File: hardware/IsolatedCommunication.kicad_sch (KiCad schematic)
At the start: 4 parts, among them U13 LTC6820IMS

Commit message: added additional USB port and overall board update
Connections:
- net MSIO renamed MISO
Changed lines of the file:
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@@
     (effects (font (size 1.27 1.27)) (justify right))
   )
-  (hierarchical_label "MSIO" (shape output) (at 118.745 85.725 180)
+  (hierarchical_label "MISO" (shape output) (at 118.745 85.725 180)
     (effects (font (size 1.27 1.27)) (justify right))
   )
@@
   (symbol (lib_id "power:+3.3V") (at 120.015 78.105 0)
     (in_bom yes) (on_board yes)
-    (property "Reference" "#PWR?" (id 0) (at 120.015 81.915 0)
+    (property "Reference" "#PWR0144" (id 0) (at 120.015 81.915 0)
       (effects (font (size 1.27 1.27)) hide)
     )
@@
   (symbol (lib_id "power:GND") (at 145.415 107.95 0)
     (in_bom yes) (on_board yes)
-    (property "Reference" "#PWR?" (id 0) (at 145.415 114.3 0)
+    (property "Reference" "#PWR0143" (id 0) (at 145.415 114.3 0)
       (effects (font (size 1.27 1.27)) hide)
     )
@@
   (symbol (lib_id "power:+3.3V") (at 142.875 78.105 0)
     (in_bom yes) (on_board yes)
-    (property "Reference" "#PWR?" (id 0) (at 142.875 81.915 0)
+    (property "Reference" "#PWR0145" (id 0) (at 142.875 81.915 0)
       (effects (font (size 1.27 1.27)) hide)
     )

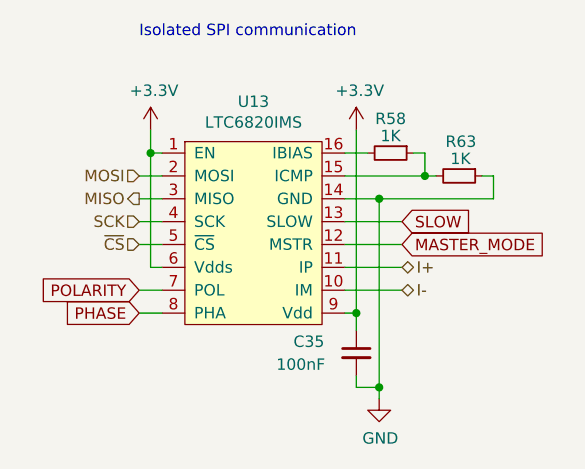
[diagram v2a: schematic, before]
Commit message: Schematic readability update
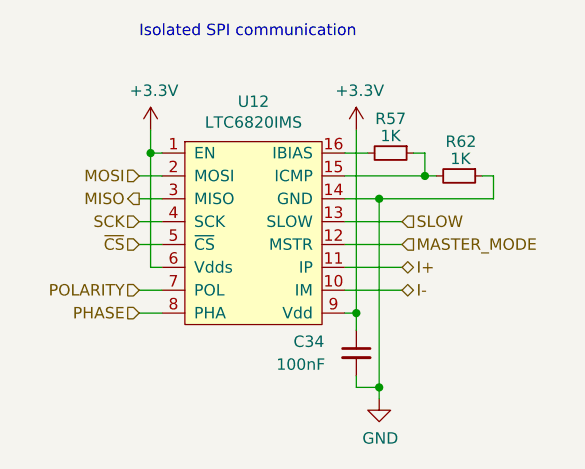
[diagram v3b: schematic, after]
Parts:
- renumbered C35 to C34, R58 to R57, R63 to R62, U13 to U12
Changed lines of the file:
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@@
     (effects (font (size 1.27 1.27)) (justify left bottom))
   )
-  (global_label "SLOW" (shape input) (at 147.955 88.265 0) (fields_autoplaced)
+  (hierarchical_label "SLOW" (shape input) (at 147.955 88.265 0)
     (effects (font (size 1.27 1.27)) (justify left))
-    (property "Intersheet References" "${INTERSHEET_REFS}" (id 0) (at 155.2987 88.1856 0)
-      (effects (font (size 1.27 1.27)) (justify left) hide)
-    )
-  )
-  (global_label "PHASE" (shape input) (at 118.745 98.425 180) (fields_autoplaced)
-    (effects (font (size 1.27 1.27)) (justify right))
-    (property "Intersheet References" "${INTERSHEET_REFS}" (id 0) (at 110.3732 98.3456 0)
-      (effects (font (size 1.27 1.27)) (justify right) hide)
-    )
-  )
-  (global_label "MASTER_MODE" (shape input) (at 147.955 90.805 0) (fields_autoplaced)
-    (effects (font (size 1.27 1.27)) (justify left))
-    (property "Intersheet References" "${INTERSHEET_REFS}" (id 0) (at 163.584 90.7256 0)
-      (effects (font (size 1.27 1.27)) (justify left) hide)
-    )
-  )
-  (global_label "POLARITY" (shape input) (at 118.745 95.885 180) (fields_autoplaced)
-    (effects (font (size 1.27 1.27)) (justify right))
-    (property "Intersheet References" "${INTERSHEET_REFS}" (id 0) (at 107.7727 95.8056 0)
-      (effects (font (size 1.27 1.27)) (justify right) hide)
-    )
   )
   (hierarchical_label "SCK" (shape input) (at 118.745 88.265 180)
@@
     (effects (font (size 1.27 1.27)) (justify right))
   )
+  (hierarchical_label "MASTER_MODE" (shape input) (at 147.955 90.805 0)
+    (effects (font (size 1.27 1.27)) (justify left))
+  )
   (hierarchical_label "MOSI" (shape input) (at 118.745 83.185 180)
     (effects (font (size 1.27 1.27)) (justify right))
   )
+  (hierarchical_label "POLARITY" (shape input) (at 118.745 95.885 180)
+    (effects (font (size 1.27 1.27)) (justify right))
+  )
   (hierarchical_label "MISO" (shape output) (at 118.745 85.725 180)
+    (effects (font (size 1.27 1.27)) (justify right))
+  )
+  (hierarchical_label "PHASE" (shape input) (at 118.745 98.425 180)
     (effects (font (size 1.27 1.27)) (justify right))
   )
@@
   (symbol (lib_id "power:+3.3V") (at 120.015 78.105 0)
     (in_bom yes) (on_board yes)
-    (property "Reference" "#PWR0144" (id 0) (at 120.015 81.915 0)
+    (property "Reference" "#PWR0141" (id 0) (at 120.015 81.915 0)
       (effects (font (size 1.27 1.27)) hide)
     )
@@
   (symbol (lib_id "power:GND") (at 145.415 107.95 0)
     (in_bom yes) (on_board yes)
-    (property "Reference" "#PWR0143" (id 0) (at 145.415 114.3 0)
+    (property "Reference" "#PWR0140" (id 0) (at 145.415 114.3 0)
       (effects (font (size 1.27 1.27)) hide)
     )
@@
   (symbol (lib_id "PUTM_EV_BMS_library:LTC6820IMS") (at 131.445 89.535 0)
     (in_bom yes) (on_board yes)
-    (property "Reference" "U13" (id 0) (at 131.445 74.93 0))
+    (property "Reference" "U12" (id 0) (at 131.445 74.93 0))
     (property "Value" "LTC6820IMS" (id 1) (at 131.445 77.2414 0))
     (property "Footprint" "Package_SO:MSOP-16_3x4.039mm_P0.5mm" (id 2) (at 131.445 103.505 0)
@@
   (symbol (lib_id "power:+3.3V") (at 142.875 78.105 0)
     (in_bom yes) (on_board yes)
-    (property "Reference" "#PWR0145" (id 0) (at 142.875 81.915 0)
+    (property "Reference" "#PWR0142" (id 0) (at 142.875 81.915 0)
       (effects (font (size 1.27 1.27)) hide)
     )
@@
   (symbol (lib_id "Device:R_Small") (at 154.305 83.185 270)
     (in_bom yes) (on_board yes)
-    (property "Reference" "R63" (id 0) (at 156.21 79.375 90)
+    (property "Reference" "R62" (id 0) (at 156.21 79.375 90)
       (effects (font (size 1.27 1.27)) (justify right))
     )
@@
   (symbol (lib_id "Device:R_Small") (at 146.685 80.645 270)
     (in_bom yes) (on_board yes)
-    (property "Reference" "R58" (id 0) (at 146.685 76.835 90))
+    (property "Reference" "R57" (id 0) (at 146.685 76.835 90))
     (property "Value" "1K" (id 1) (at 146.685 78.74 90))
     (property "Footprint" "Resistor_SMD:R_0603_1608Metric" (id 2) (at 146.685 80.645 0)
@@
   (symbol (lib_id "Device:C_Small") (at 142.875 102.87 0)
     (in_bom yes) (on_board yes)
-    (property "Reference" "C35" (id 0) (at 135.89 101.6 0)
+    (property "Reference" "C34" (id 0) (at 135.89 101.6 0)
       (effects (font (size 1.27 1.27)) (justify left))
     )

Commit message: finished pcb layout, started routing, changed 2 layered board to 4 layered'
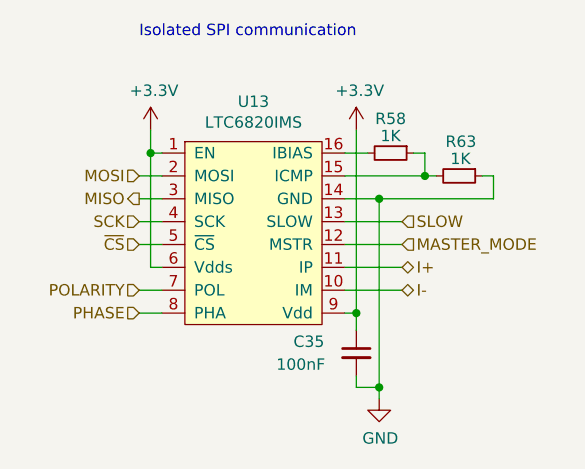
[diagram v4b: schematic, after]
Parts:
- renumbered C34 to C35, R57 to R58, R62 to R63, U12 to U13
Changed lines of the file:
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@@
   (symbol (lib_id "power:+3.3V") (at 120.015 78.105 0)
     (in_bom yes) (on_board yes)
-    (property "Reference" "#PWR0141" (id 0) (at 120.015 81.915 0)
+    (property "Reference" "#PWR0144" (id 0) (at 120.015 81.915 0)
       (effects (font (size 1.27 1.27)) hide)
     )
@@
   (symbol (lib_id "power:GND") (at 145.415 107.95 0)
     (in_bom yes) (on_board yes)
-    (property "Reference" "#PWR0140" (id 0) (at 145.415 114.3 0)
+    (property "Reference" "#PWR0143" (id 0) (at 145.415 114.3 0)
       (effects (font (size 1.27 1.27)) hide)
     )
@@
   (symbol (lib_id "PUTM_EV_BMS_library:LTC6820IMS") (at 131.445 89.535 0)
     (in_bom yes) (on_board yes)
-    (property "Reference" "U12" (id 0) (at 131.445 74.93 0))
+    (property "Reference" "U13" (id 0) (at 131.445 74.93 0))
     (property "Value" "LTC6820IMS" (id 1) (at 131.445 77.2414 0))
     (property "Footprint" "Package_SO:MSOP-16_3x4.039mm_P0.5mm" (id 2) (at 131.445 103.505 0)
@@
   (symbol (lib_id "power:+3.3V") (at 142.875 78.105 0)
     (in_bom yes) (on_board yes)
-    (property "Reference" "#PWR0142" (id 0) (at 142.875 81.915 0)
+    (property "Reference" "#PWR0145" (id 0) (at 142.875 81.915 0)
       (effects (font (size 1.27 1.27)) hide)
     )
@@
   (symbol (lib_id "Device:R_Small") (at 154.305 83.185 270)
     (in_bom yes) (on_board yes)
-    (property "Reference" "R62" (id 0) (at 156.21 79.375 90)
+    (property "Reference" "R63" (id 0) (at 156.21 79.375 90)
       (effects (font (size 1.27 1.27)) (justify right))
     )
@@
   (symbol (lib_id "Device:R_Small") (at 146.685 80.645 270)
     (in_bom yes) (on_board yes)
-    (property "Reference" "R57" (id 0) (at 146.685 76.835 90))
+    (property "Reference" "R58" (id 0) (at 146.685 76.835 90))
     (property "Value" "1K" (id 1) (at 146.685 78.74 90))
     (property "Footprint" "Resistor_SMD:R_0603_1608Metric" (id 2) (at 146.685 80.645 0)
@@
   (symbol (lib_id "Device:C_Small") (at 142.875 102.87 0)
     (in_bom yes) (on_board yes)
-    (property "Reference" "C34" (id 0) (at 135.89 101.6 0)
+    (property "Reference" "C35" (id 0) (at 135.89 101.6 0)
       (effects (font (size 1.27 1.27)) (justify left))
     )

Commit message: remake in progress
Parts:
- renumbered C35 to C34, R58 to R57, R63 to R62, U13 to U12
